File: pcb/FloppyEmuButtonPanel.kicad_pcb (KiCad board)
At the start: 2 copper layers, 45.3 x 33.3 mm, 13 parts, among them J1 ButtonPanelConnector, SW1 PREVIOUS/UP, SW2 SELECT, SW3 NEXT/DOWN, SW4 RESET

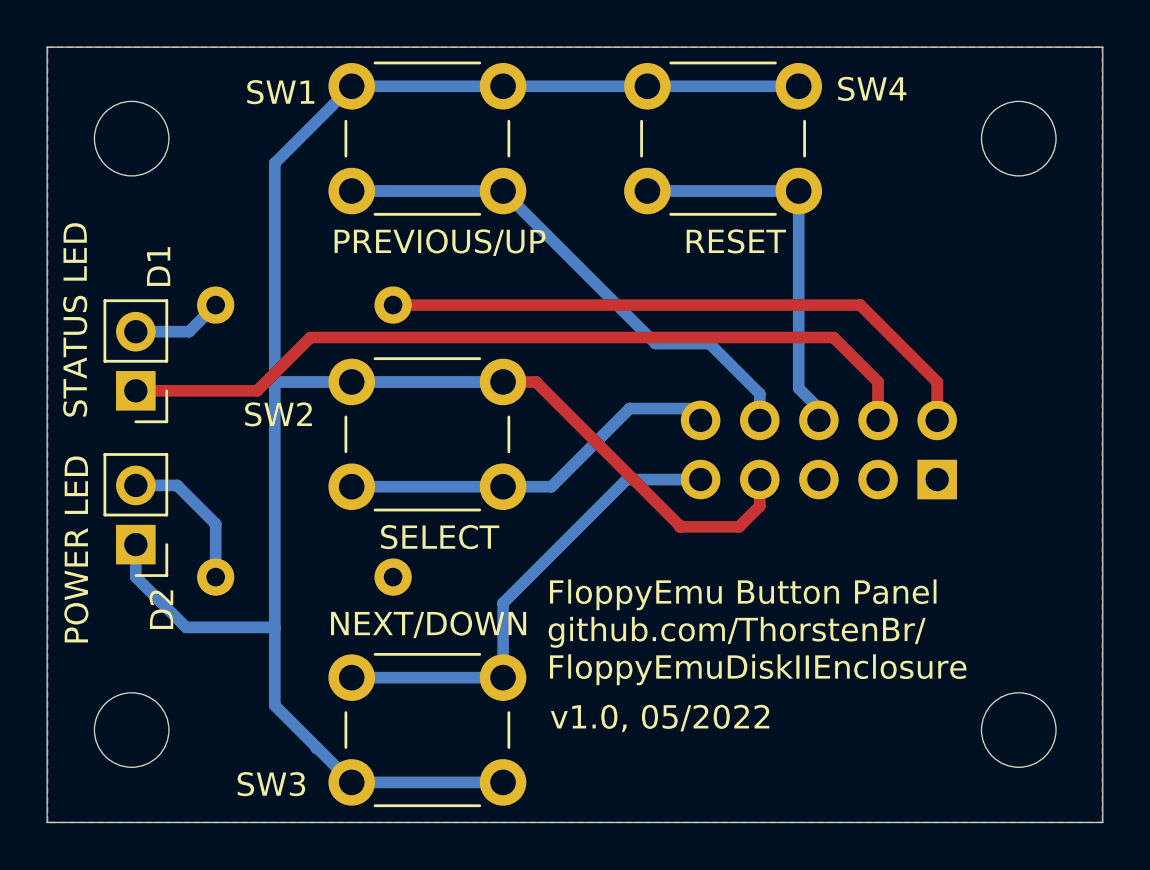
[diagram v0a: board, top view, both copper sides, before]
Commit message: Corrected button panel (mounting points). Added Gerber files for PCB.
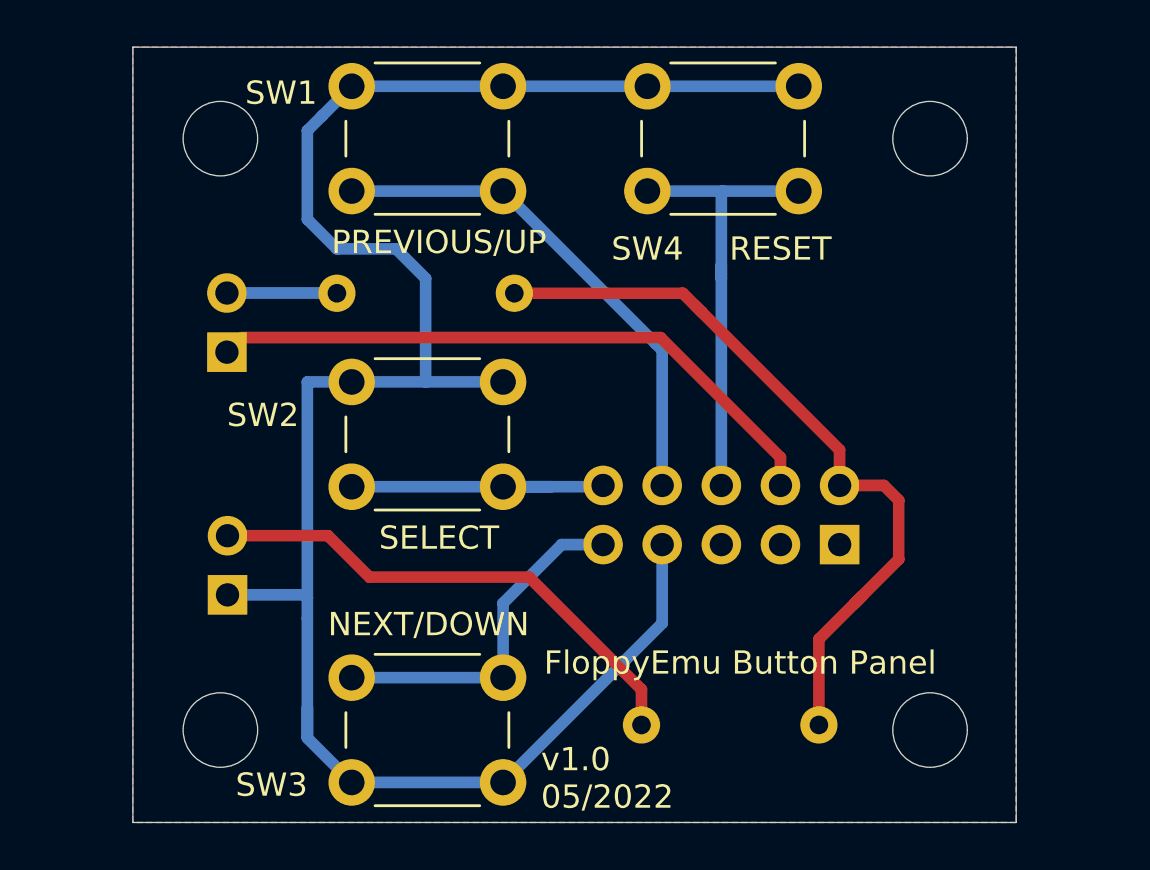
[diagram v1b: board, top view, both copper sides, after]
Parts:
- D1: value STATUS LED -> STATUS; moved to B.Cu
- D2: value POWER LED -> POWER; moved to B.Cu
- moved R2 19.4 mm to (131.8, 96.0)
- moved R1 5.23 mm to (118.7, 77.5)
- moved J1 5.04 mm to (132.7, 88.3)
- moved D2 4.49 mm to (106.4, 90.4), turned to 0 degrees
- moved D1 4.25 mm to (106.4, 80.0), turned to 0 degrees
- moved H1 3.81 mm to (106.1, 96.2)
- moved H2 3.81 mm to (106.1, 70.8)
- moved H3 3.81 mm to (136.6, 70.8)
- moved H4 3.81 mm to (136.6, 96.2)
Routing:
- net GND: track 149.1 -> 106.2 mm
- net Net-(D2-Pad2): track 6.40 -> 22.0 mm
- net /STATUS: track 34.8 -> 27.4 mm
- net +5V: track 25.9 -> 33.1 mm
- net /NEXT: track 20.9 -> 15.0 mm
- net /RESET: track 16.2 -> 19.7 mm
- net /SELECT: track 16.9 -> 13.3 mm
- net Net-(D1-Pad2): track 3.90 -> 4.73 mm
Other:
- board size 45.3 x 33.3 mm -> 37.9 x 33.3 mm
- board text added: "+"
- board text added: "-"
- board text added: "FloppyEmu Button Panel"
- board text added: "github.com/ThorstenBr/ FloppyEmuDiskIIEnclosure"
- board text added: "v1.0 05/2022"
- board text removed: "FloppyEmu Button Panel github.com/ThorstenBr/ FloppyEmuDiskIIEnclosure"
- board text removed: "v1.0, 05/2022"
